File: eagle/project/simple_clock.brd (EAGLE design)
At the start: 100 x 80 mm, 7 parts, among them IC1 MAX7219CNG

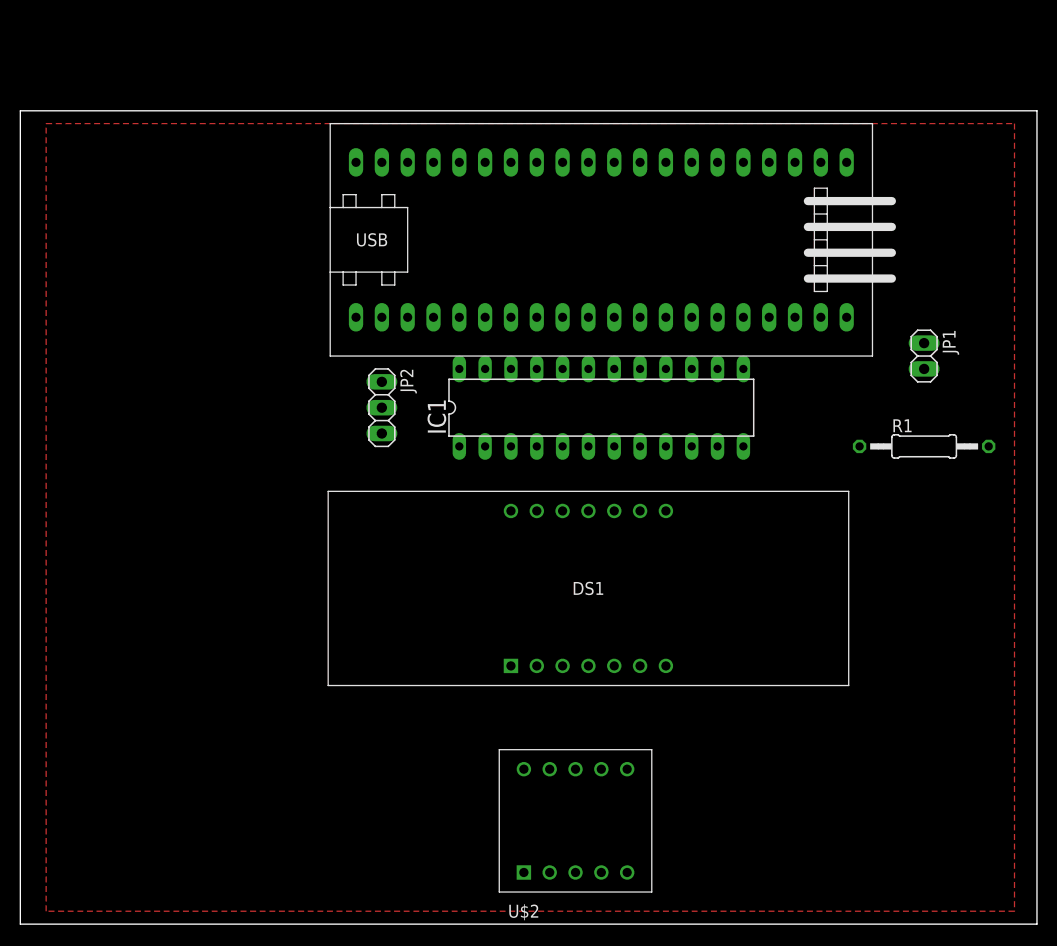
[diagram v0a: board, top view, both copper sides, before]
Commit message: made pcb in Eagle
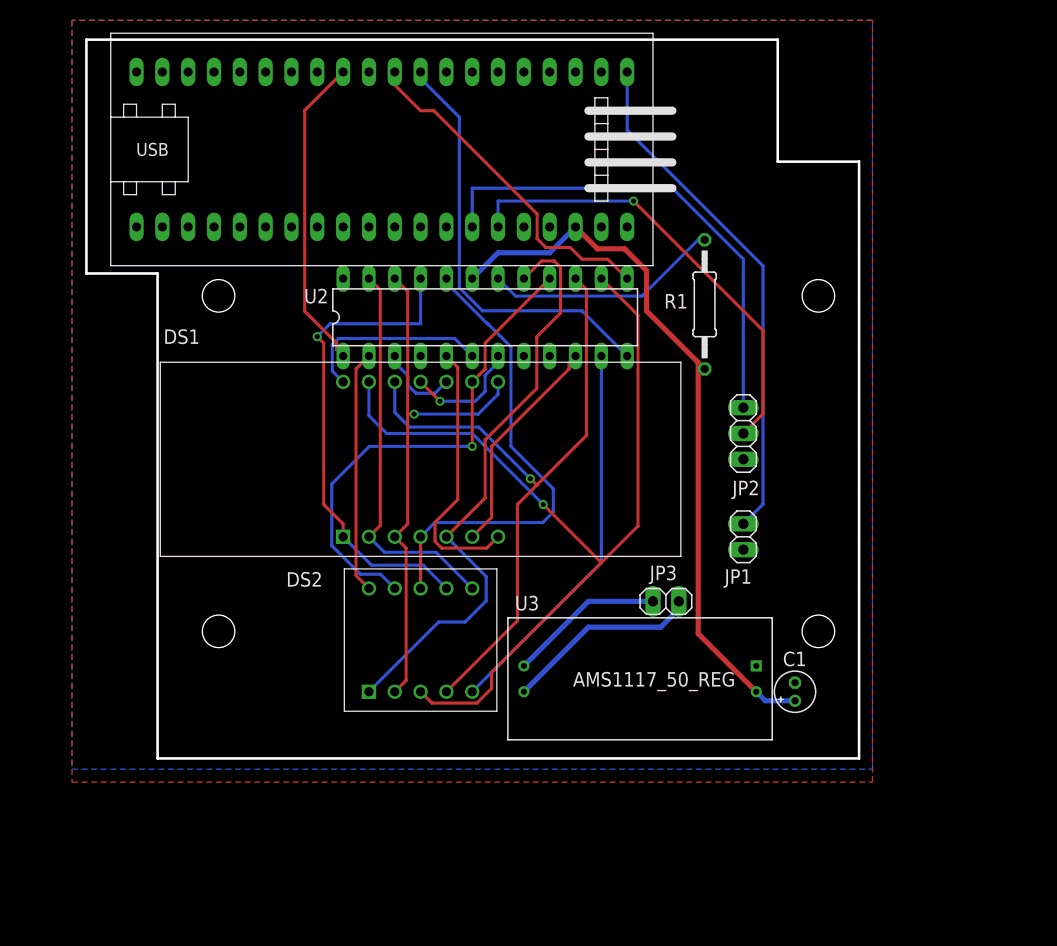
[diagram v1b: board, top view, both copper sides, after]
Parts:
- removed IC1: MAX7219CNG, maxim:DIL24-3
- removed U$1: STM32F103C8T6-MODULE, stm32f103c8t6_module:STM32F103C8T6-MODULE
- removed U$2: F3261AH, clock-7-seg:F3261AH
- added C1: 4.7u, rcl:E1,8-4
- added DS2: F3261AH, simple_clock:F3261AH
- added JP3: (no value), pinhead:1X02
- added U1: STM32F103C8T6-MODULE, stm32f103c8t6_module:STM32F103C8T6-MODULE
- added U2: MAX7219CNG, maxim:DIL24-3
- added U3: AMS1117_50_REG, simple_clock:AMS1117_50_REG
- DS1: device clock-7-seg:F5463AH -> simple_clock:F5463AH
- moved JP2 35.7 mm to (71.1, 48.3), turned to 90 degrees
- moved R1 25.7 mm to (67.3, 61.0), turned to 90 degrees
- moved JP1 25.1 mm to (71.1, 38.1)
- moved DS1 22.2 mm to (39.4, 45.7)
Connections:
- removed net N$17: DS1.3, DS1.8, IC1.22, U$2.2
- new net N$23: JP3.1, U3.3
- new net N$24: JP3.2, U3.4
- new net N$25: DS1.9, DS2.9, U2.16
- net +5V: now also C1.+, U1.5V, U2.19, U3.2; no longer IC1.19, U$1.5V
- net GND: now also C1.-, U1.GND_1, U1.GND_2, U1.GND_3, U2.4, U2.9, U3.1; no longer IC1.4, IC1.9, U$1.GND_1, U$1.GND_2, U$1.GND_3
- net N$1: now also U2.3; no longer IC1.3
- net N$10: now also U1.PA_4, U2.12; no longer IC1.12, U$1.PA_4
- net N$11: now also DS2.3, U2.14; no longer IC1.14, U$2.3, U$2.9
- net N$12: now also DS2.7, U2.21; no longer IC1.21, U$2.7
- net N$13: now also DS1.3, DS1.8, DS2.2, U2.22; no longer DS1.9, IC1.16
- net N$14: now also DS2.4, U2.15; no longer IC1.15, U$2.4
- net N$15: now also DS2.8, U2.20; no longer IC1.20, U$2.8
- net N$16: now also DS2.6, U2.23; no longer IC1.23, U$2.6
- net N$18: now also DS2.1, U2.17; no longer IC1.17, U$2.1
- net N$19: now also U2.18; no longer IC1.18
- net N$2: now also U2.5; no longer IC1.5
- net N$20: now also U1.VB; no longer U$1.VB
- net N$21: now also U1.PB_7; no longer U$1.PB_7
- net N$22: now also U1.PB_6; no longer U$1.PB_6
- net N$3: now also U1.PA_7, U2.1; no longer IC1.1, U$1.PA_7
- net N$4: now also U2.6; no longer IC1.6
- net N$5: now also DS2.10, U2.2; no longer IC1.2, U$2.10
- net N$6: now also DS2.5, U2.11; no longer IC1.11, U$2.5
- net N$7: now also U2.7; no longer IC1.7
- net N$8: now also U2.10; no longer IC1.10
- net N$9: now also U1.PA_5, U2.13; no longer IC1.13, U$1.PA_5
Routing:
- net N$11: track 0.00 -> 88.0 mm, vias 0 -> 1
- net +5V: track 0.00 -> 72.0 mm
- net N$14: track 0.00 -> 66.7 mm, vias 0 -> 1
- net N$18: track 0.00 -> 58.9 mm
- net N$13: track 0.00 -> 53.5 mm, vias 0 -> 1
- net N$20: track 0.00 -> 50.8 mm
- net N$25: track 0.00 -> 49.0 mm, vias 0 -> 1
- net N$12: track 0.00 -> 48.1 mm, vias 0 -> 1
- net N$22: track 0.00 -> 48.0 mm
- net N$15: track 0.00 -> 46.5 mm
- net N$21: track 0.00 -> 44.8 mm, vias 0 -> 1
- net N$10: track 0.00 -> 42.1 mm
- net N$16: track 0.00 -> 38.6 mm
- net N$6: track 0.00 -> 38.3 mm
- net N$9: track 0.00 -> 33.4 mm
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- added copper zone on layer 16, net GND
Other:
- board size 100 x 80 mm -> 76 x 70.7 mm
- board text added: "B1 B2 Gnd"
- board text added: "Gnd"
- board text added: "VBatt"
- board text added: "Vin +9VDC"

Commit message: created Gerber files
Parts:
- moved C1 0.90 mm to (76.3, 23.7)
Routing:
- net GND: track 0.00 -> 131.5 mm
- net N$14: track 66.7 -> 100.8 mm, vias 1 -> 0
- net N$18: track 58.9 -> 86.3 mm
- net N$19: track 23.3 -> 40.6 mm
- net N$13: track 53.5 -> 70.5 mm, vias 1 -> 0
- net N$15: track 46.5 -> 32.6 mm
- net N$25: track 49.0 -> 37.8 mm, vias 1 -> 0
- net N$12: track 48.1 -> 55.5 mm, vias 1 -> 0
- net N$11: track 88.0 -> 82.0 mm, vias 1 -> 0
- net N$8: track 22.0 -> 27.5 mm
- net N$22: track 48.0 -> 43.4 mm
- net N$21: track 44.8 -> 41.3 mm, vias 1 -> 0
- net N$4: track 18.8 -> 15.7 mm
- net N$1: track 7.98 -> 10.5 mm
- net N$16: track 38.6 -> 40.8 mm
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- removed copper zone on layer 1, net GND
- removed copper zone on layer 16, net GND
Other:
- board text added: "VBatt Gnd"
- board text removed: "VBatt"

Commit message: ready to make pcb
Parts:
- moved JP2 4.58 mm to (73.7, 52.1), flipped to the bottom
- moved JP1 2.84 mm to (73.7, 39.4), flipped to the bottom
- moved R1 1.80 mm to (68.6, 59.7)
- moved U1 1.42 mm to (35.6, 75.6)
- moved DS1 1.27 mm to (40.6, 45.7)
- moved DS2 1.27 mm to (40.6, 27.9)
- moved JP3 1.27 mm to (62.2, 31.8), flipped to the bottom, turned to 180 degrees
- moved U2 1.27 mm to (47.0, 59.7)
- moved U3 1.27 mm to (62.2, 24.1)
- moved C1 1.20 mm to (77.5, 24.1)
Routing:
- net N$18: track 86.3 -> 51.1 mm, vias 0 -> 1
- net N$25: track 37.8 -> 72.5 mm
- net N$5: track 23.9 -> 51.3 mm, vias 0 -> 1
- net N$14: track 100.8 -> 85.2 mm
- net N$19: track 40.6 -> 26.1 mm
- net N$9: track 34.3 -> 46.8 mm
- net N$11: track 82.0 -> 69.6 mm, vias 0 -> 2
- net N$12: track 55.5 -> 43.3 mm
- net N$2: track 26.7 -> 20.3 mm
- net N$8: track 27.5 -> 22.0 mm
- net GND: track 131.5 -> 135.7 mm, vias 0 -> 1
- net N$24: track 19.7 -> 16.6 mm
- net N$4: track 15.7 -> 18.8 mm
- net N$10: track 41.9 -> 44.9 mm, vias 0 -> 1
- net N$3: track 31.1 -> 28.4 mm
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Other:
- board size 76 x 70.7 mm -> 75.5 x 70.7 mm
- board text added: "Vbatt Gnd"
- board text added: "simple_clock v.2 by Palis Ratanaswasd"
- board text removed: "VBatt Gnd"

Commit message: updated board design
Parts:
- moved JP1 1.27 mm to (72.4, 39.4)
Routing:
- net GND: track 135.7 -> 146.3 mm, vias 1 -> 0
- net N$18: track 51.1 -> 60.9 mm, vias 1 -> 0
- net N$22: track 41.9 -> 51.6 mm
- net N$5: track 51.3 -> 60.9 mm, vias 1 -> 0
- net N$21: track 40.7 -> 48.7 mm
- net N$19: track 26.1 -> 33.2 mm
- net N$10: track 44.9 -> 49.4 mm
- net N$25: track 72.5 -> 76.1 mm
- net N$1: track 8.21 -> 10.8 mm
- net N$3: track 28.4 -> 30.5 mm, vias 0 -> 1
- net +5V: track 70.0 -> 71.9 mm
- net N$7: track 11.0 -> 12.6 mm, vias 1 -> 0
- net N$13: track 71.4 -> 73.0 mm
- net N$4: track 18.8 -> 20.0 mm
- net N$14: track 85.2 -> 86.0 mm
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
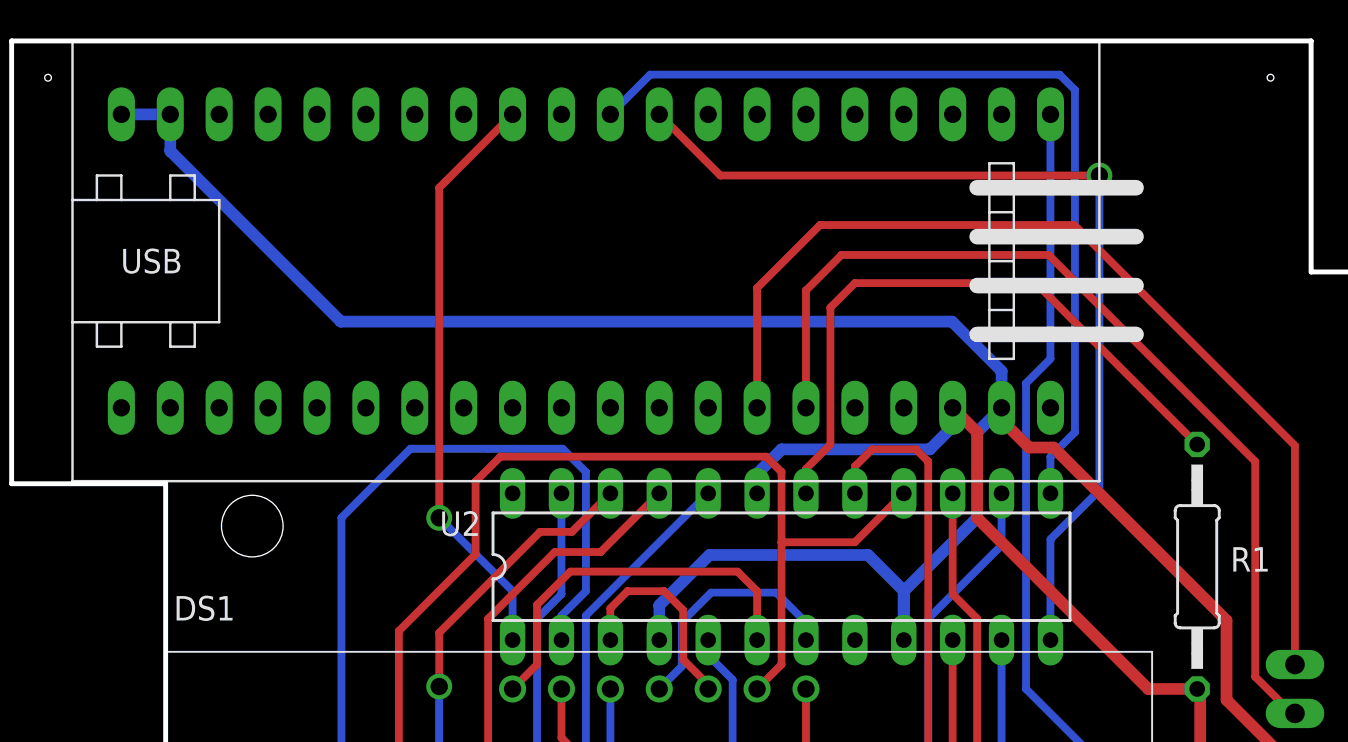
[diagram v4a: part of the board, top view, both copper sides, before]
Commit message: updated footprints
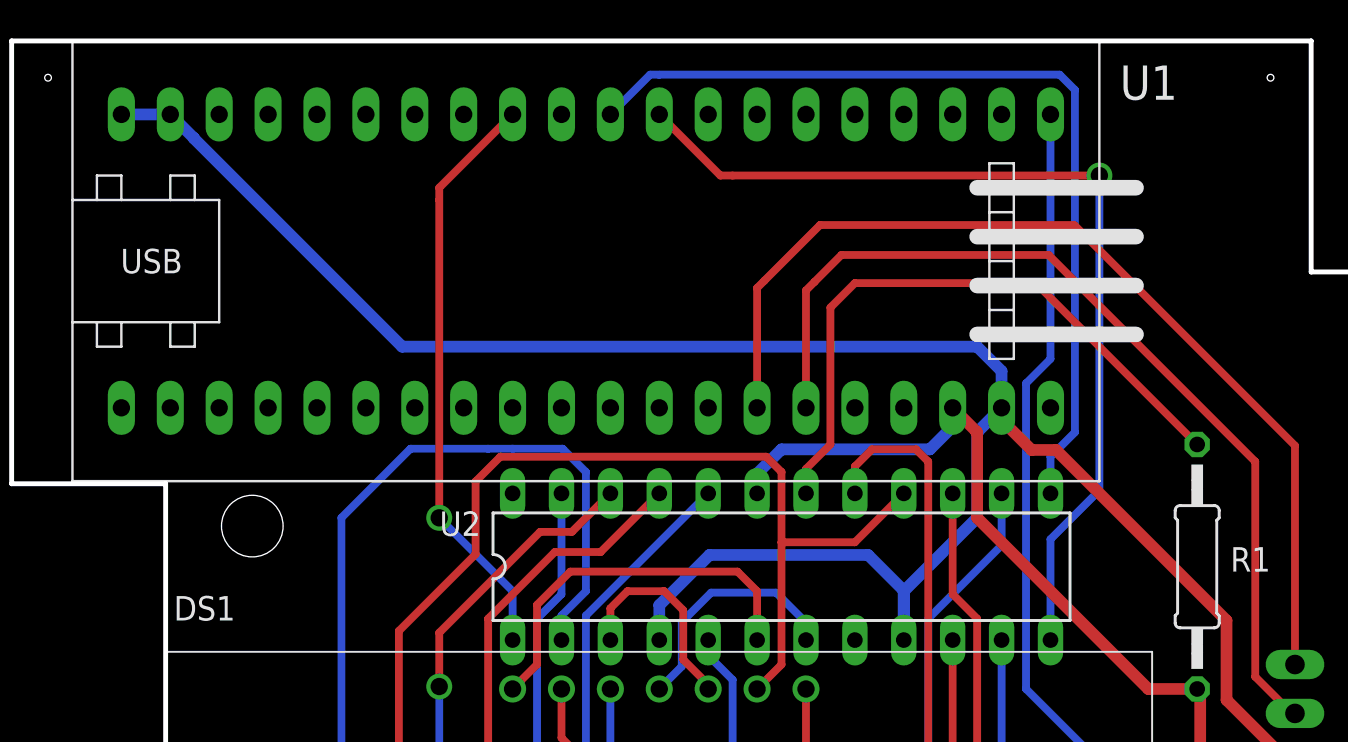
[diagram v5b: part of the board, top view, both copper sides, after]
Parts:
- U1: value STM32F103C8T6-MODULE -> STM32F103C8T6; device stm32f103c8t6_module:STM32F103C8T6-MODULE -> stm32f103c8t6_module:STM32F103C8T6
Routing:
- net GND: track 146.3 -> 145.2 mm
